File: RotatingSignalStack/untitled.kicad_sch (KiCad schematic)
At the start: 1 part

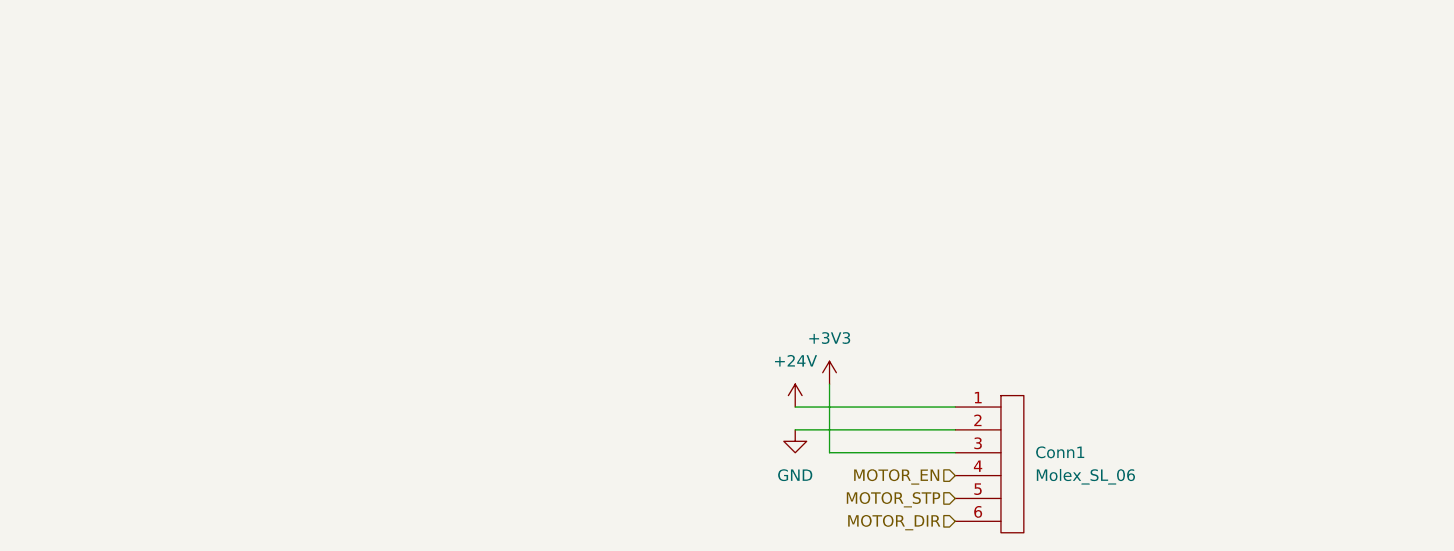
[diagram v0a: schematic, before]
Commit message: STM designed (mostly), ESD and pin linking next
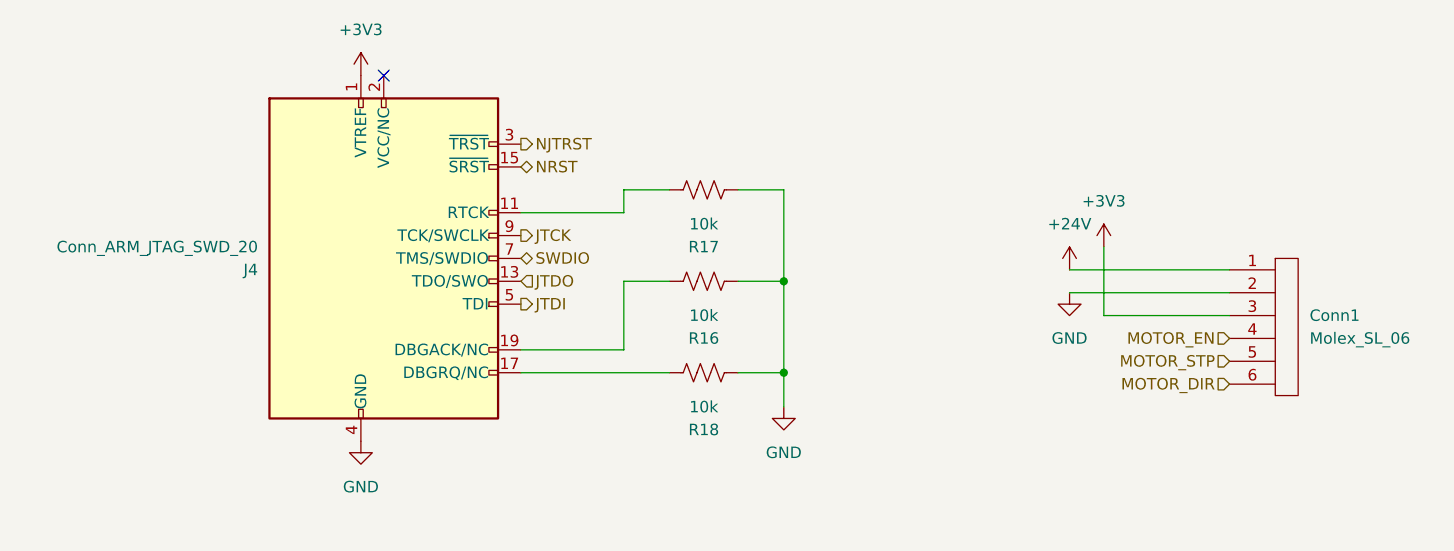
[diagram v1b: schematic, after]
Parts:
- added J4: Conn_ARM_JTAG_SWD_20, symbol Connector:Conn_ARM_JTAG_SWD_20
- added R16, R17, R18: 10k, symbol Device:R_US
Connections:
- net +3V3: now also J4.1 (VTREF)
- net GND: now also J4.10 (GND), J4.12 (GND), J4.14 (GND), J4.16 (GND), J4.18 (GND), J4.20 (GND), J4.4 (GND), J4.6 (GND), J4.8 (GND), R16.1, R17.1, R18.1
- new net: J4.11 (RTCK), R17.2
- new net: J4.17 (DBGRQ/NC), R18.2
- new net: J4.19 (DBGACK/NC), R16.2
- new net JTCK: J4.9 (TCK/SWCLK)
- new net JTDI: J4.5 (TDI)
- new net JTDO: J4.13 (TDO/SWO)
- new net NJTRST: J4.3 (~{TRST})
- new net NRST: J4.15 (~{SRST})
- new net SWDIO: J4.7 (TMS/SWDIO)
- no-connect marks 0 -> 1
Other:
- moved on the sheet: Conn1
